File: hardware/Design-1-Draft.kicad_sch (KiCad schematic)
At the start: 54 parts, among them J1 Barrel_Jack_Switch, M1 WP-1, M2 WP-2, Q1 IRLZ44N, Q2 IRLZ44N, Q3 PN2222A, SW1 Button, U3 ADS1115, U5 Tang_Nano_9K, U7 BOB-12009

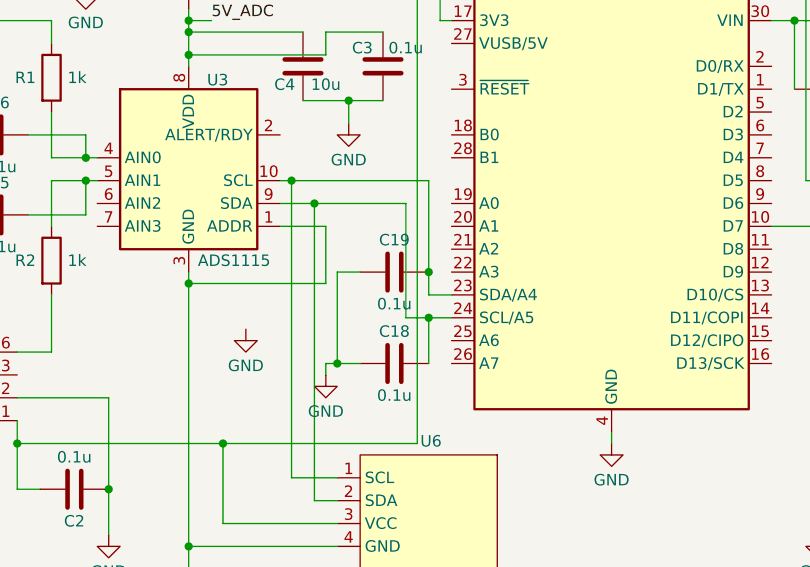
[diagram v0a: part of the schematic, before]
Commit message: Updated schem & PCB, caps not removed
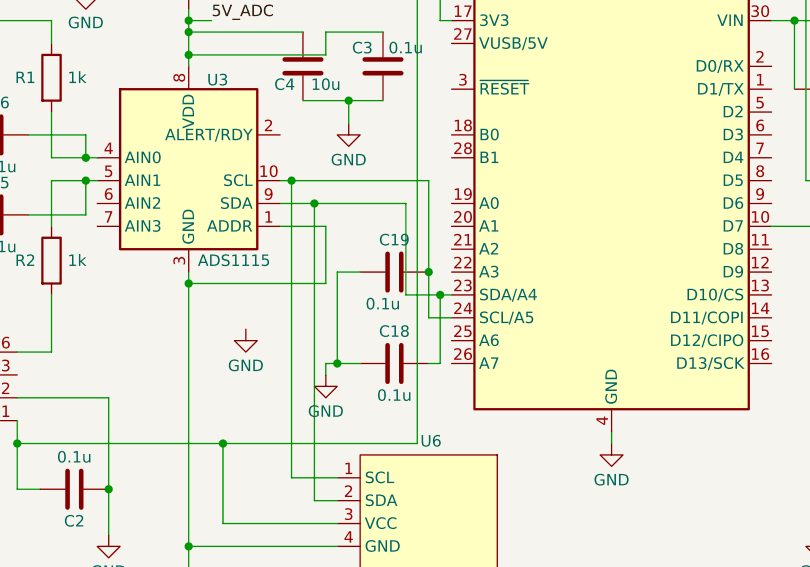
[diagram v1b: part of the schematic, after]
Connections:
- net at C18.2, U3.9 (SDA), U6.2 (SDA): now also A1.23 (SDA/A4); no longer A1.24 (SCL/A5)
- net at C19.2, U3.10 (SCL), U6.1 (SCL): now also A1.24 (SCL/A5); no longer A1.23 (SDA/A4)
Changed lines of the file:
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@@
 	)
 	(junction
-		(at 86.36 90.17)
+		(at 223.52 76.2)
 		(diameter 0)
 		(color 0 0 0 0)
 	)
 	(junction
-		(at 223.52 76.2)
+		(at 102.87 43.18)
 		(diameter 0)
 		(color 0 0 0 0)
 	)
 	(junction
-		(at 102.87 43.18)
+		(at 59.69 86.36)
 		(diameter 0)
 		(color 0 0 0 0)
 	)
 	(junction
-		(at 59.69 86.36)
+		(at 87.63 87.63)
 		(diameter 0)
 		(color 0 0 0 0)
@@
 	(wire
 		(pts
+			(xy 86.36 90.17) (xy 88.9 90.17)
+		)
+		(stroke
+			(width 0)
+			(type default)
+		)
+	)
+	(wire
+		(pts
 			(xy 59.69 86.36) (xy 59.69 115.57)
 		)
@@
 	(wire
 		(pts
+			(xy 87.63 87.63) (xy 87.63 95.25)
+		)
+		(stroke
+			(width 0)
+			(type default)
+		)
+	)
+	(wire
+		(pts
 			(xy 223.52 76.2) (xy 224.79 76.2)
 		)
@@
 	(wire
 		(pts
-			(xy 86.36 90.17) (xy 86.36 95.25)
-		)
-		(stroke
-			(width 0)
-			(type default)
-		)
-	)
-	(wire
-		(pts
 			(xy 223.52 44.45) (xy 223.52 76.2)
 		)
@@
 	(wire
 		(pts
-			(xy 86.36 90.17) (xy 88.9 90.17)
-		)
-		(stroke
-			(width 0)
-			(type default)
-		)
-	)
-	(wire
-		(pts
 			(xy 93.98 27.94) (xy 97.79 27.94)
 		)
@@
 	(wire
 		(pts
-			(xy 156.21 105.41) (xy 161.29 105.41)
+			(xy 86.36 85.09) (xy 86.36 90.17)
 		)
 		(stroke
@@
 	(wire
 		(pts
-			(xy 50.8 30.48) (xy 54.61 30.48)
+			(xy 156.21 105.41) (xy 161.29 105.41)
 		)
 		(stroke
@@
 	(wire
 		(pts
-			(xy 128.27 41.91) (xy 121.92 41.91)
+			(xy 50.8 30.48) (xy 54.61 30.48)
 		)
 		(stroke
@@
 	(wire
 		(pts
-			(xy 48.26 52.07) (xy 48.26 53.34)
+			(xy 128.27 41.91) (xy 121.92 41.91)
 		)
 		(stroke
@@
 	(wire
 		(pts
-			(xy 214.63 69.85) (xy 236.22 69.85)
+			(xy 48.26 52.07) (xy 48.26 53.34)
 		)
 		(stroke
@@
 	(wire
 		(pts
-			(xy 59.69 60.96) (xy 59.69 62.23)
+			(xy 214.63 69.85) (xy 236.22 69.85)
 		)
 		(stroke
@@
 	(wire
 		(pts
-			(xy 83.82 90.17) (xy 86.36 90.17)
+			(xy 59.69 60.96) (xy 59.69 62.23)
 		)
 		(stroke
@@
 	(wire
 		(pts
-			(xy 85.09 45.72) (xy 121.92 45.72)
+			(xy 87.63 95.25) (xy 86.36 95.25)
 		)
 		(stroke
@@
 	(wire
 		(pts
-			(xy 219.71 92.71) (xy 233.68 92.71)
+			(xy 85.09 45.72) (xy 121.92 45.72)
 		)
 		(stroke
@@
 	(wire
 		(pts
-			(xy 77.47 66.04) (xy 77.47 68.58)
+			(xy 219.71 92.71) (xy 233.68 92.71)
 		)
 		(stroke
@@
 	(wire
 		(pts
-			(xy 133.35 41.91) (xy 133.35 57.15)
+			(xy 77.47 66.04) (xy 77.47 68.58)
 		)
 		(stroke
@@
 	(wire
 		(pts
-			(xy 78.74 95.25) (xy 76.2 95.25)
+			(xy 133.35 41.91) (xy 133.35 57.15)
 		)
 		(stroke
@@
 	(wire
 		(pts
-			(xy 83.82 77.47) (xy 83.82 90.17)
+			(xy 83.82 77.47) (xy 83.82 87.63)
 		)
 		(stroke
@@
 	(wire
 		(pts
-			(xy 86.36 87.63) (xy 88.9 87.63)
+			(xy 161.29 59.69) (xy 160.02 59.69)
 		)
 		(stroke
@@
 	(wire
 		(pts
-			(xy 161.29 59.69) (xy 160.02 59.69)
+			(xy 97.79 33.02) (xy 111.76 33.02)
 		)
 		(stroke
@@
 	(wire
 		(pts
-			(xy 97.79 33.02) (xy 111.76 33.02)
+			(xy 254 81.28) (xy 254 107.95)
 		)
 		(stroke
@@
 	(wire
 		(pts
-			(xy 254 81.28) (xy 254 107.95)
+			(xy 74.93 86.36) (xy 59.69 86.36)
 		)
 		(stroke
@@
 	(wire
 		(pts
-			(xy 74.93 86.36) (xy 59.69 86.36)
+			(xy 88.9 57.15) (xy 87.63 57.15)
 		)
 		(stroke
@@
 	(wire
 		(pts
-			(xy 88.9 57.15) (xy 87.63 57.15)
+			(xy 57.15 49.53) (xy 57.15 45.72)
 		)
 		(stroke
@@
 	(wire
 		(pts
-			(xy 57.15 49.53) (xy 57.15 45.72)
+			(xy 59.69 58.42) (xy 59.69 60.96)
 		)
 		(stroke
@@
 	(wire
 		(pts
-			(xy 59.69 58.42) (xy 59.69 60.96)
+			(xy 87.63 87.63) (xy 88.9 87.63)
 		)
 		(stroke
@@
 	(wire
 		(pts
+			(xy 83.82 87.63) (xy 87.63 87.63)
+		)
+		(stroke
+			(width 0)
+			(type default)
+		)
+	)
+	(wire
+		(pts
+			(xy 78.74 95.25) (xy 76.2 95.25)
+		)
+		(stroke
+			(width 0)
+			(type default)
+		)
+	)
+	(wire
+		(pts
 			(xy 69.85 74.93) (xy 71.12 74.93)
 		)
@@
 	(wire
 		(pts
-			(xy 86.36 85.09) (xy 86.36 87.63)
-		)
-		(stroke
-			(width 0)
-			(type default)
-		)
-	)
-	(wire
-		(pts
 			(xy 43.18 109.22) (xy 40.64 109.22)
 		)
@@
 		)
 		(property "Value" "0.1u"
-			(at 82.55 88.646 90)
+			(at 81.28 88.646 90)
 			(effects
 				(font

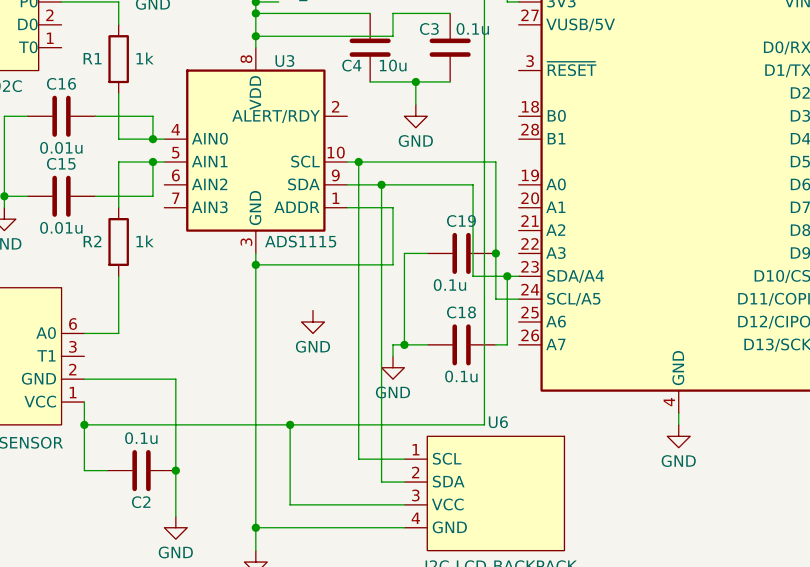
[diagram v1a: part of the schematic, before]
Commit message: Updated schem and PCB, switched SDA & SCL lines on arduino pins, removed filter caps @ arduino pins
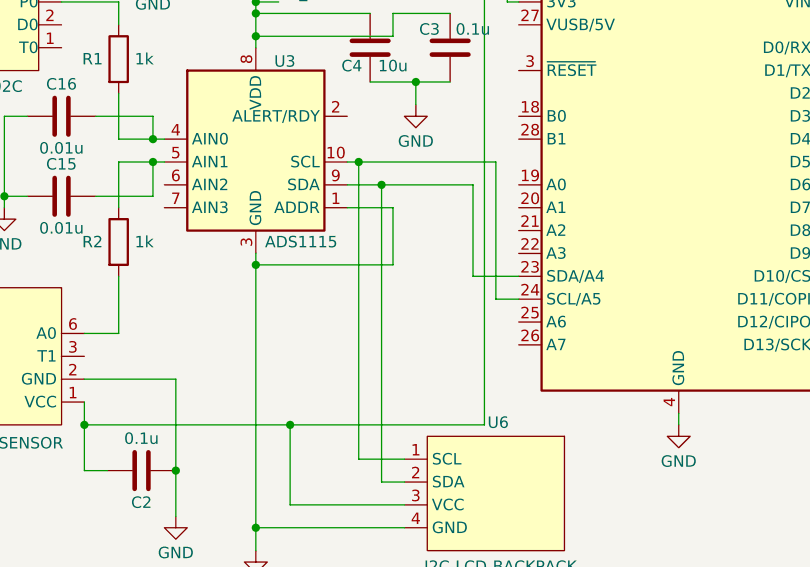
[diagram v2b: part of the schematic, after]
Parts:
- removed C18, C19: 0.1u, Capacitor_THT:C_Disc_D5.0mm_W2.5mm_P5.00mm, symbol Device:C
